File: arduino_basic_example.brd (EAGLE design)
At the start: 56.6 x 38.9 mm, 23 parts, among them IC1 ATMEGA328P, Q1 16mhz

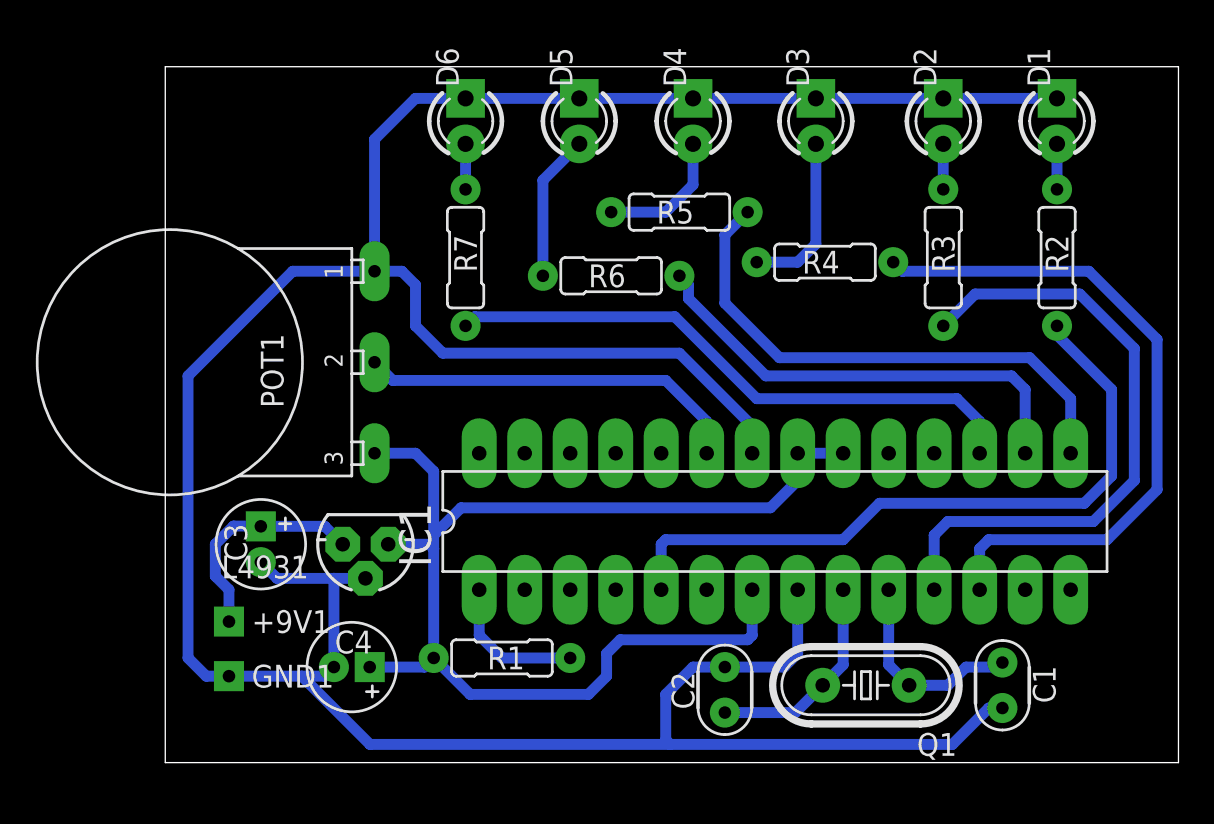
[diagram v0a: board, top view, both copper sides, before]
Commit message: update regulator label
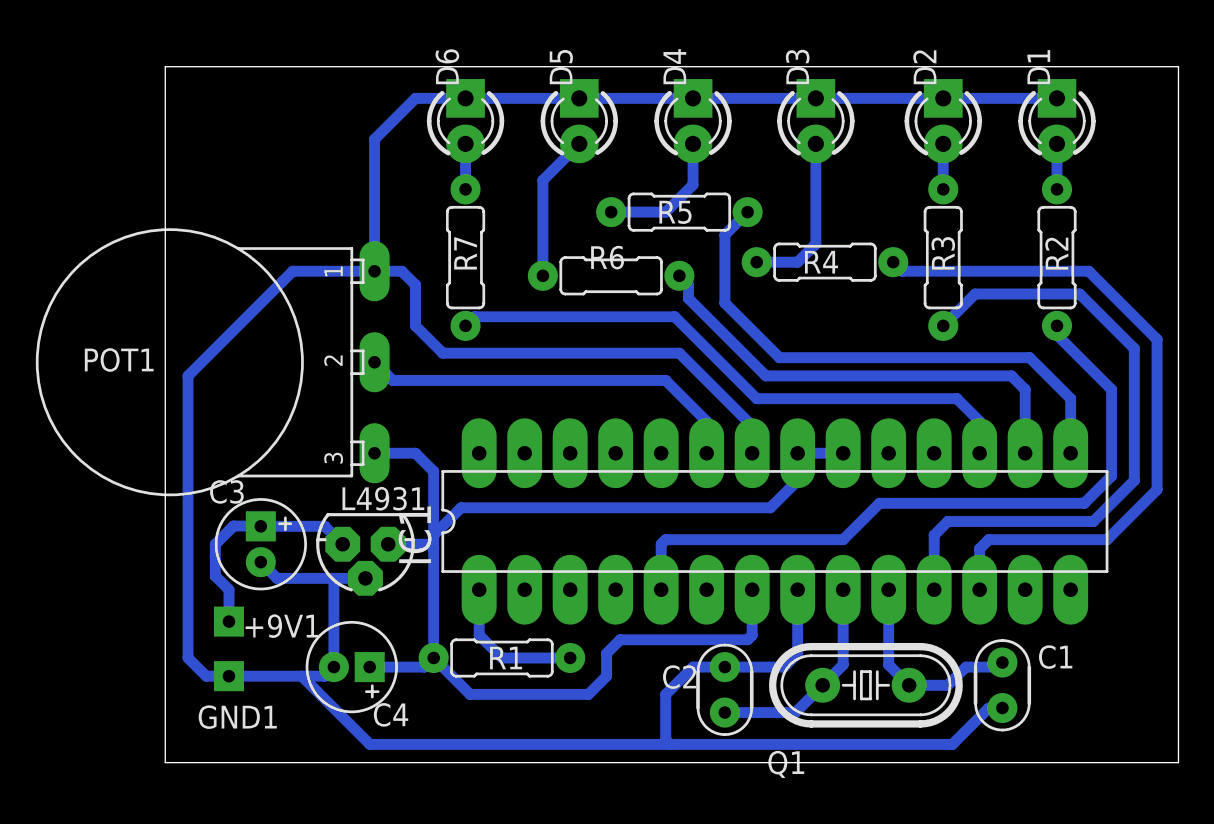
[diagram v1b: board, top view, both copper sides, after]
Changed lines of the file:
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@@
 </autorouter>
 <elements>
-<element name="+9V1" library="gm-supply" package="SQUARE" value="+9V(T)" x="3.556" y="7.874"/>
-<element name="C1" library="gm-caps-ceramic" package="050X030_025" value="22pf" x="46.736" y="4.318" rot="R270"/>
-<element name="C2" library="gm-caps-ceramic" package="050X030_025" value="22pf" x="31.242" y="4.064" rot="R90"/>
-<element name="C3" library="gm-caps-electro-pol" package="050_020" value="2.2uf" x="5.334" y="12.192" rot="R270"/>
-<element name="C4" library="gm-caps-electro-pol" package="050_020" value="2.2uf" x="10.414" y="5.334" rot="R180"/>
-<element name="D1" library="gm-diodes" package="LED3MM" value="LED3MM" x="49.784" y="35.814" rot="R90"/>
-<element name="D2" library="gm-diodes" package="LED3MM" value="LED3MM" x="43.434" y="35.814" rot="R90"/>
-<element name="D3" library="gm-diodes" package="LED3MM" value="LED3MM" x="36.322" y="35.814" rot="R90"/>
-<element name="D4" library="gm-diodes" package="LED3MM" value="LED3MM" x="29.464" y="35.814" rot="R90"/>
-<element name="D5" library="gm-diodes" package="LED3MM" value="LED3MM" x="23.114" y="35.814" rot="R90"/>
-<element name="D6" library="gm-diodes" package="LED3MM" value="LED3MM" x="16.764" y="35.814" rot="R90"/>
-<element name="GND1" library="gm-supply" package="SQUARE" value="GND(T)" x="3.556" y="4.826"/>
+<element name="+9V1" library="gm-supply" package="SQUARE" value="+9V(T)" x="3.556" y="7.874" smashed="yes">
+<attribute name="NAME" x="4.318" y="6.985" size="1.27" layer="25" ratio="12"/>
+</element>
+<element name="C1" library="gm-caps-ceramic" package="050X030_025" value="22pf" x="46.736" y="4.318" smashed="yes" rot="R270">
+<attribute name="NAME" x="48.6918" y="5.2578" size="1.27" layer="25" ratio="12"/>
+<attribute name="VALUE" x="48.8804" y="3.2258" size="1.27" layer="27" ratio="12"/>
+</element>
+<element name="C2" library="gm-caps-ceramic" package="050X030_025" value="22pf" x="31.242" y="4.064" smashed="yes" rot="R90">
+<attribute name="NAME" x="29.7942" y="5.4102" size="1.27" layer="25" ratio="12" rot="R180"/>
+<attribute name="VALUE" x="29.6056" y="3.3782" size="1.27" layer="27" ratio="12" rot="R180"/>
+</element>
+<element name="C3" library="gm-caps-electro-pol" package="050_020" value="2.2uf" x="5.334" y="12.192" smashed="yes" rot="R270">
+<attribute name="NAME" x="2.413" y="14.478" size="1.27" layer="25" ratio="12"/>
+<attribute name="VALUE" x="5.334" y="14.605" size="1.27" layer="27" ratio="12"/>
+</element>
+<element name="C4" library="gm-caps-electro-pol" package="050_020" value="2.2uf" x="10.414" y="5.334" smashed="yes" rot="R180">
+<attribute name="NAME" x="11.557" y="2.032" size="1.27" layer="25" ratio="12"/>
+<attribute name="VALUE" x="17.78" y="2.921" size="1.27" layer="27" ratio="12" rot="R180"/>
+</element>
+<element name="D1" library="gm-diodes" package="LED3MM" value="LED3MM" x="49.784" y="35.814" smashed="yes" rot="R90">
+<attribute name="NAME" x="49.403" y="37.719" size="1.27" layer="25" ratio="12" rot="R90"/>
+<attribute name="VALUE" x="51.435" y="37.719" size="1.27" layer="27" ratio="12" rot="R90"/>
+</element>
+<element name="D2" library="gm-diodes" package="LED3MM" value="LED3MM" x="43.434" y="35.814" smashed="yes" rot="R90">
+<attribute name="NAME" x="43.053" y="37.719" size="1.27" layer="25" ratio="12" rot="R90"/>
+<attribute name="VALUE" x="45.085" y="37.719" size="1.27" layer="27" ratio="12" rot="R90"/>
+</element>
+<element name="D3" library="gm-diodes" package="LED3MM" value="LED3MM" x="36.322" y="35.814" smashed="yes" rot="R90">
+<attribute name="NAME" x="35.941" y="37.719" size="1.27" layer="25" ratio="12" rot="R90"/>
+<attribute name="VALUE" x="37.973" y="37.719" size="1.27" layer="27" ratio="12" rot="R90"/>
+</element>
+<element name="D4" library="gm-diodes" package="LED3MM" value="LED3MM" x="29.464" y="35.814" smashed="yes" rot="R90">
+<attribute name="NAME" x="29.083" y="37.719" size="1.27" layer="25" ratio="12" rot="R90"/>
+<attribute name="VALUE" x="31.115" y="37.719" size="1.27" layer="27" ratio="12" rot="R90"/>
+</element>
+<element name="D5" library="gm-diodes" package="LED3MM" value="LED3MM" x="23.114" y="35.814" smashed="yes" rot="R90">
+<attribute name="NAME" x="22.733" y="37.719" size="1.27" layer="25" ratio="12" rot="R90"/>
+<attribute name="VALUE" x="24.765" y="37.719" size="1.27" layer="27" ratio="12" rot="R90"/>
+</element>
+<element name="D6" library="gm-diodes" package="LED3MM" value="LED3MM" x="16.764" y="35.814" smashed="yes" rot="R90">
+<attribute name="NAME" x="16.383" y="37.719" size="1.27" layer="25" ratio="12" rot="R90"/>
+<attribute name="VALUE" x="18.415" y="37.719" size="1.27" layer="27" ratio="12" rot="R90"/>
+</element>
+<element name="GND1" library="gm-supply" package="SQUARE" value="GND(T)" x="3.556" y="4.826" smashed="yes">
+<attribute name="NAME" x="1.778" y="1.905" size="1.27" layer="25" ratio="12"/>
+</element>
 <element name="IC1" library="atmel" package="DIL28-3" value="ATMEGA328P" x="34.036" y="13.462">
 <attribute name="MPN" value="" x="34.036" y="13.462" size="1.778" layer="27" display="off"/>
@@
 <attribute name="MF" value="" x="34.036" y="13.462" size="1.778" layer="27" display="off"/>
 </element>
-<element name="L4931" library="v-reg-3" package="78LXX" value="5v" x="11.176" y="12.192" rot="R180"/>
-<element name="POT1" library="gm-pots" package="16MM" value="10k" x="11.684" y="22.352" rot="R90"/>
-<element name="Q1" library="adafruit" package="HC49/S" value="16mhz" x="39.116" y="4.318" rot="R180">
+<element name="L4931" library="v-reg-3" package="78LXX" value="5v" x="11.176" y="12.192" smashed="yes" rot="R180">
+<attribute name="NAME" x="14.605" y="15.367" size="1.27" layer="25" ratio="10" rot="R180"/>
+<attribute name="VALUE" x="14.097" y="10.668" size="1.27" layer="27" ratio="10" rot="R180"/>
+</element>
+<element name="POT1" library="gm-pots" package="16MM" value="10k" x="11.684" y="22.352" smashed="yes" rot="R90">
+<attribute name="NAME" x="-0.508" y="23.114" size="1.27" layer="25" ratio="12" rot="R180"/>
+<attribute name="VALUE" x="-2.286" y="25.527" size="1.27" layer="27" ratio="12" rot="R180"/>
+</element>
+<element name="Q1" library="adafruit" package="HC49/S" value="16mhz" x="39.116" y="4.318" smashed="yes" rot="R180">
 <attribute name="MPN" value="" x="39.116" y="4.318" size="1.778" layer="27" rot="R180" display="off"/>
 <attribute name="OC_NEWARK" value="unknown" x="39.116" y="4.318" size="1.778" layer="27" rot="R180" display="off"/>
 <attribute name="OC_FARNELL" value="1667008" x="39.116" y="4.318" size="1.778" layer="27" rot="R180" display="off"/>
 <attribute name="MF" value="" x="39.116" y="4.318" size="1.778" layer="27" rot="R180" display="off"/>
+<attribute name="NAME" x="35.814" y="0.635" size="1.27" layer="25" ratio="10" rot="R180"/>
+<attribute name="VALUE" x="41.402" y="0.635" size="1.27" layer="27" ratio="10" rot="R180"/>
 </element>
-<element name="R1" library="gm-resistors" package="R0207/3" value="10k" x="18.796" y="5.842" rot="R180"/>
-<element name="R2" library="gm-resistors" package="R0207/3" value="300" x="49.784" y="28.194" rot="R270"/>
-<element name="R3" library="gm-resistors" package="R0207/3" value="300" x="43.434" y="28.194" rot="R270"/>
-<element name="R4" library="gm-resistors" package="R0207/3" value="300" x="36.83" y="27.94"/>
-<element name="R5" library="gm-resistors" package="R0207/3" value="300" x="28.702" y="30.734"/>
-<element name="R6" library="gm-resistors" package="R0207/3" value="300" x="24.892" y="27.178"/>
-<element name="R7" library="gm-resistors" package="R0207/3" value="300" x="16.764" y="28.194" rot="R270"/>
+<element name="R1" library="gm-resistors" package="R0207/3" value="10k" x="18.796" y="5.842" smashed="yes" rot="R180">
+<attribute name="NAME" x="20.066" y="6.477" size="1.27" layer="25" font="vector" ratio="12" rot="R180"/>
+<attribute name="VALUE" x="20.066" y="8.382" size="1.27" layer="27" font="vector" ratio="12" rot="R180"/>
+</element>
+<element name="R2" library="gm-resistors" package="R0207/3" value="300" x="49.784" y="28.194" smashed="yes" rot="R270">
+<attribute name="NAME" x="49.149" y="29.464" size="1.27" layer="25" font="vector" ratio="12" rot="R270"/>
+<attribute name="VALUE" x="47.244" y="29.464" size="1.27" layer="27" font="vector" ratio="12" rot="R270"/>
+</element>
+<element name="R3" library="gm-resistors" package="R0207/3" value="300" x="43.434" y="28.194" smashed="yes" rot="R270">
+<attribute name="NAME" x="42.799" y="29.464" size="1.27" layer="25" font="vector" ratio="12" rot="R270"/>
+<attribute name="VALUE" x="40.894" y="29.464" size="1.27" layer="27" font="vector" ratio="12" rot="R270"/>
+</element>
+<element name="R4" library="gm-resistors" package="R0207/3" value="300" x="36.83" y="27.94" smashed="yes">
+<attribute name="NAME" x="35.56" y="27.305" size="1.27" layer="25" font="vector" ratio="12"/>
+<attribute name="VALUE" x="35.56" y="25.4" size="1.27" layer="27" font="vector" ratio="12"/>
+</element>
+<element name="R5" library="gm-resistors" package="R0207/3" value="300" x="28.702" y="30.734" smashed="yes">
+<attribute name="NAME" x="27.432" y="30.099" size="1.27" layer="25" font="vector" ratio="12"/>
+<attribute name="VALUE" x="27.432" y="28.194" size="1.27" layer="27" font="vector" ratio="12"/>
+</element>
+<element name="R6" library="gm-resistors" package="R0207/3" value="300" x="24.892" y="27.178" smashed="yes">
+<attribute name="NAME" x="23.622" y="27.559" size="1.27" layer="25" font="vector" ratio="12"/>
+<attribute name="VALUE" x="23.368" y="25.654" size="1.27" layer="27" font="vector" ratio="12"/>
+</element>
+<element name="R7" library="gm-resistors" package="R0207/3" value="300" x="16.764" y="28.194" smashed="yes" rot="R270">
+<attribute name="NAME" x="16.129" y="29.464" size="1.27" layer="25" font="vector" ratio="12" rot="R270"/>
+<attribute name="VALUE" x="14.224" y="29.464" size="1.27" layer="27" font="vector" ratio="12" rot="R270"/>
+</element>
 </elements>
 <signals>

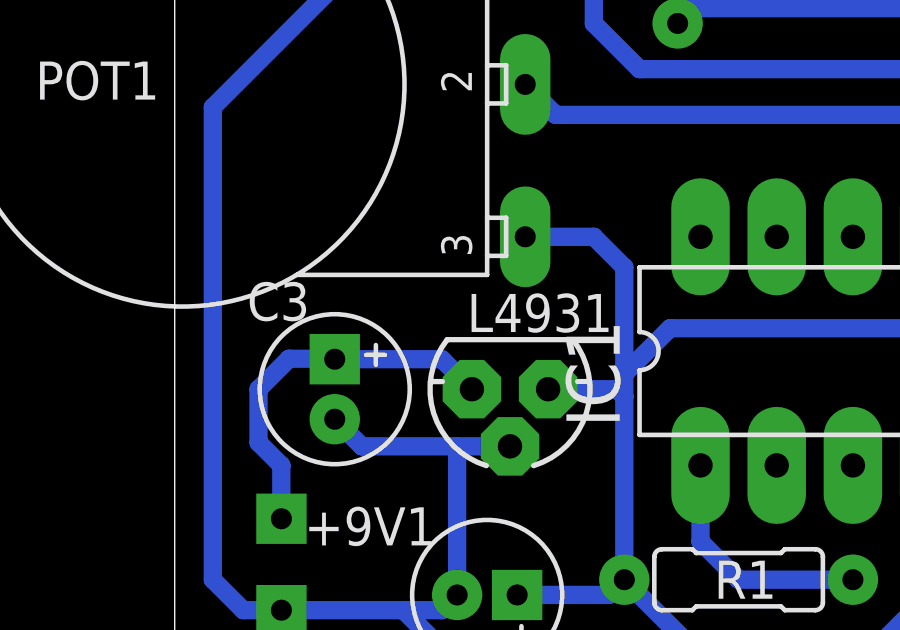
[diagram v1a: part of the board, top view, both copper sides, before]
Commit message: update regulator label
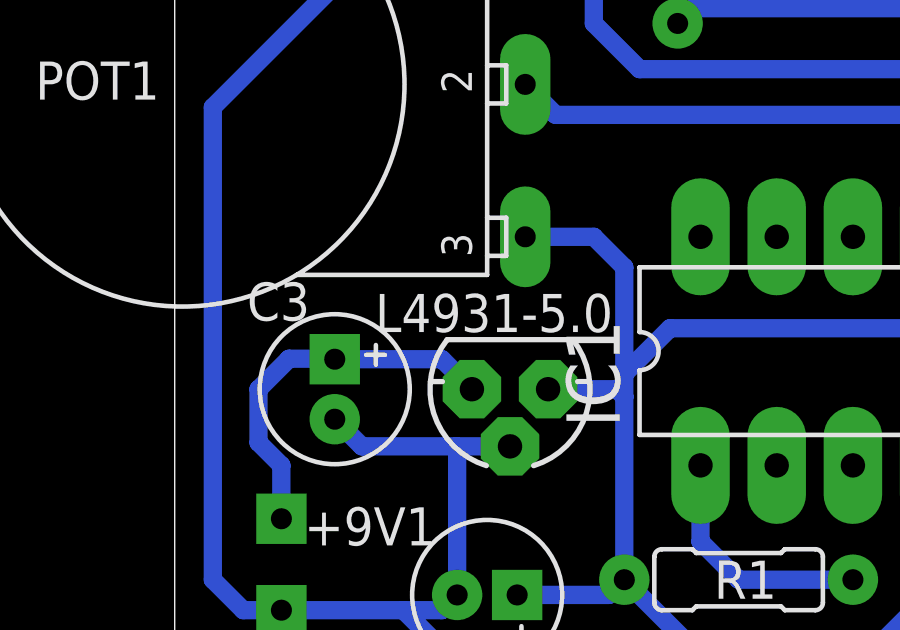
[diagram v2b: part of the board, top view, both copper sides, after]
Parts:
- L4931-5.0: value 5v -> 5v reg
- renumbered L4931 to L4931-5.0
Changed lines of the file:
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@@
 <attribute name="MF" value="" x="34.036" y="13.462" size="1.778" layer="27" display="off"/>
 </element>
-<element name="L4931" library="v-reg-3" package="78LXX" value="5v" x="11.176" y="12.192" smashed="yes" rot="R180">
+<element name="L4931-5.0" library="v-reg-3" package="78LXX" value="5v reg" x="11.176" y="12.192" smashed="yes" rot="R180">
 <attribute name="NAME" x="14.605" y="15.367" size="1.27" layer="25" ratio="10" rot="R180"/>
 <attribute name="VALUE" x="14.097" y="10.668" size="1.27" layer="27" ratio="10" rot="R180"/>
@@
 <contactref element="IC1" pad="21"/>
 <contactref element="IC1" pad="20"/>
-<contactref element="L4931" pad="OUT"/>
+<contactref element="L4931-5.0" pad="OUT"/>
 <contactref element="C4" pad="+"/>
 <contactref element="POT1" pad="3"/>
@@
 <contactref element="IC1" pad="22"/>
 <contactref element="GND1" pad="1"/>
-<contactref element="L4931" pad="GND"/>
+<contactref element="L4931-5.0" pad="GND"/>
 <contactref element="C3" pad="-"/>
 <contactref element="C4" pad="-"/>
@@
 <signal name="+9V">
 <contactref element="+9V1" pad="1"/>
-<contactref element="L4931" pad="IN"/>
+<contactref element="L4931-5.0" pad="IN"/>
 <contactref element="C3" pad="+"/>
 <wire x1="5.334" y1="13.192" x2="8.906" y2="13.192" width="0.6096" layer="16"/>
